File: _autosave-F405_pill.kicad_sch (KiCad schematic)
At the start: 20 parts, among them J1 Conn_01x20_Male, J2 Conn_01x20_Male, J3 USB_B_Micro, J4 Conn_01x04_Male, SW1 SW_Push, SW2 SW_Push, U1 STM32F405RGTx, U2 LM1117-3.3, U3 TJA1051T-3, Y1 Crystal_GND24

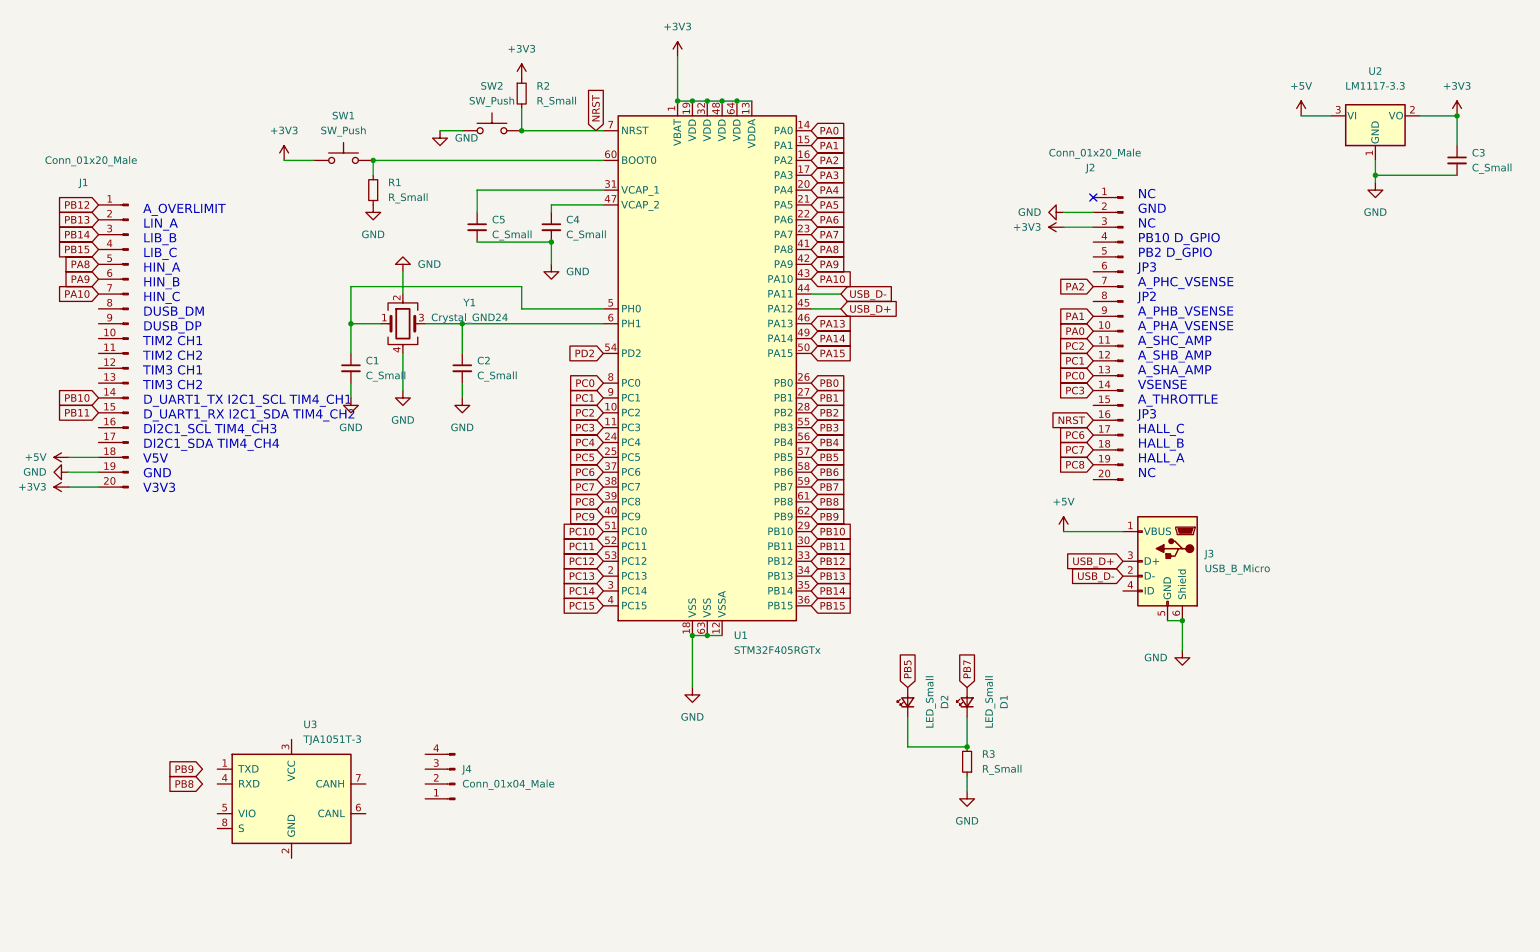
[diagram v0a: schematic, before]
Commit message: added peripherals to USB
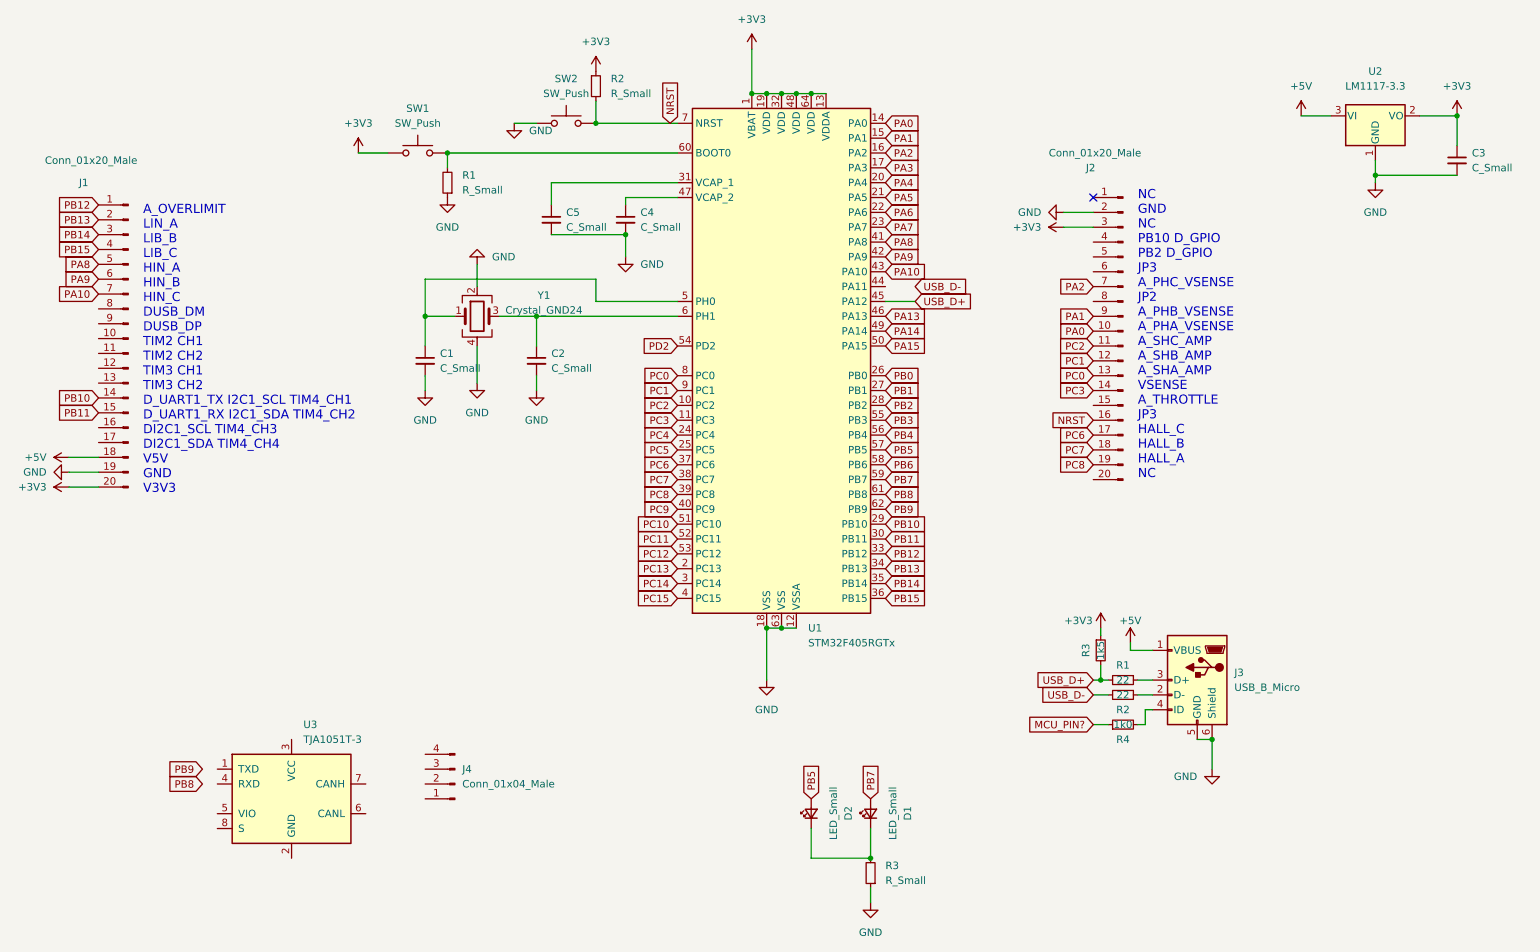
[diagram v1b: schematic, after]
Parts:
- added R1, R2: 22, Resistor_SMD:R_0603_1608Metric, symbol Device:R_Small
- added R3: 1k5, Resistor_SMD:R_0603_1608Metric, symbol Device:R_Small
- added R4: 1k0, Resistor_SMD:R_0603_1608Metric, symbol Device:R_Small
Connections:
- net +3V3: now also R3.1
- net USB_D+: now also R1.2, R3.2; no longer J3.3 (D+)
- net USB_D-: now also R2.2; no longer J3.2 (D-), U1.44 (PA11)
- net at J3.4 (ID): now also R4.2
- new net: J3.2 (D-), R2.1
- new net: J3.3 (D+), R1.1
- new net MCU_PIN?: R4.1
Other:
- moved on the sheet: C1, C2, C4, C5, D1, D2, J3, R1, R2, R3, SW1, SW2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
